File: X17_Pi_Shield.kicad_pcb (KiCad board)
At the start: 2 copper layers, 85 x 56 mm, 89 parts, among them J1 BM04B-GHS-TBT, J10 BM04B-GHS-TBT, J11 BM04B-GHS-TBT, J12 Conn_01x05_Pin, J13 Conn_01x03_Pin, J2 BM02B-GHS-TBT, J20 Conn_01x02_Pin, J22 430450212, J23 430450612, J24 430450212, J3 BM02B-GHS-TBT, J4 BM02B-GHS-TBT, J5 BM02B-GHS-TBT, J6 Conn_01x03_Pin, J7 BM04B-GHS-TBT, J8 UJC-HP-L-G-5-MSMT-TR, J9 Conn_01x03_Pin, U1 4754, U10 4754, U2 TPS2117DRLR, U3 INA260AIPW, U4 AZ1117IH-3.3TRG1, U5 MAX485, U6 MMBT3906LT3G, U7 ISOW1432BDFMR, U8 RASPBERRY_PI_4B_4GB

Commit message: Bruh
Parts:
- moved U3 0.52 mm to (175.2, 104.3)
- moved 3.3V 0.22 mm to (159.4, 94.9)
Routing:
- net GND: track 53.5 -> 120.5 mm, vias 0 -> 24
- net +3V3: track 205.7 -> 236.6 mm
- net /Pi + IMU/SCL: track 203.3 -> 210.2 mm
- net /UART/A: track 26.4 -> 32.9 mm
- net /Pi + IMU/SDA: track 186.4 -> 191.5 mm
- net +5V: track 159.4 -> 163.0 mm
- net /Pi + IMU/BKP_EN: track 78.2 -> 81.2 mm
- net Net-(U2-PR1): track 2.03 -> 4.75 mm
- net /Power/5V_TOTAL: track 44.9 -> 46.8 mm, vias 4 -> 6
- net Net-(D7-A): track 0.00 -> 1.94 mm
- net /Power/5V_BACKPLANE: track 47.2 -> 48.2 mm
- net /Power/Vs: track 22.6 -> 21.8 mm
- net /Pi + IMU/CE0: track 39.3 -> 40.1 mm
- net Net-(JP1-B): track 16.0 -> 15.3 mm
- net (no net): track 0.00 -> 0.62 mm

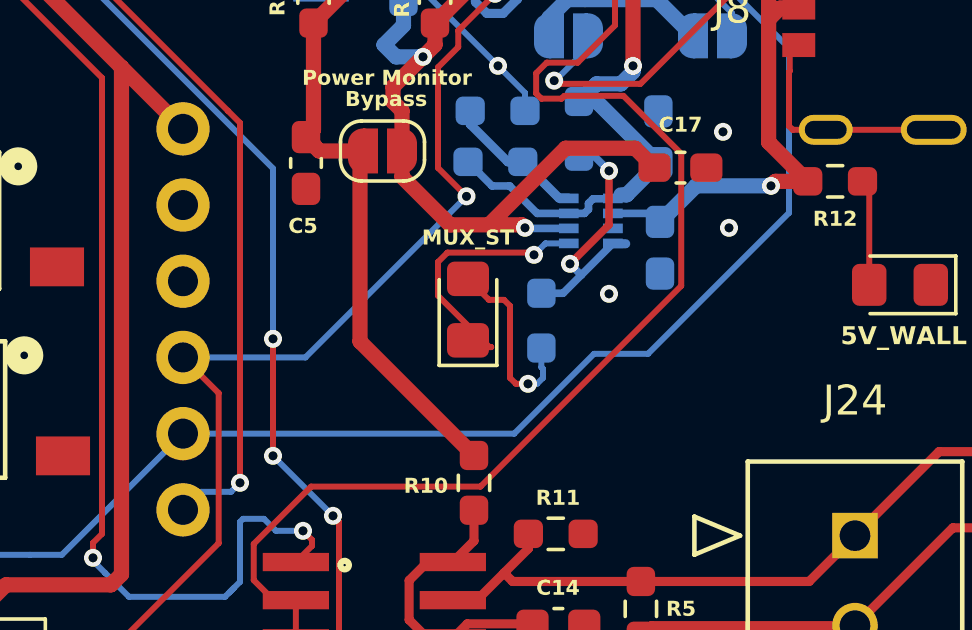
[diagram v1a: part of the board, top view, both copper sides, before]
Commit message: Unconnected Fix
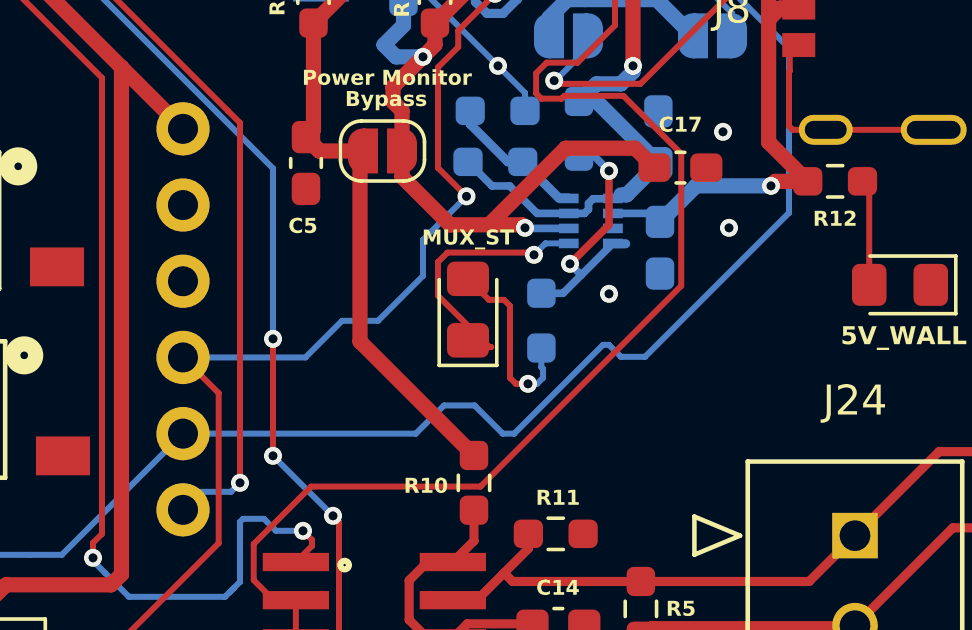
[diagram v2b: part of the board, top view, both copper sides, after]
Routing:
- net /Pi + IMU/SDA: track 191.5 -> 192.6 mm
- net /Pi + IMU/SCL: track 210.2 -> 210.9 mm
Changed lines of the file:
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@@
 	)
 	(segment
+		(start 175.1 119.7)
+		(end 175.3 119.7)
+		(width 0.2)
+		(layer "B.Cu")
+		(net 21)
+	)
+	(segment
 		(start 140.71 85.04)
 		(end 137.55 88.2)
@@
 	)
 	(segment
+		(start 181.3 109.805)
+		(end 178.07 106.575)
+		(width 0.2)
+		(layer "B.Cu")
+		(net 21)
+	)
+	(segment
+		(start 161.1 122.66)
+		(end 168.86 122.66)
+		(width 0.2)
+		(layer "B.Cu")
+		(net 21)
+	)
+	(segment
 		(start 110.3 112.5)
 		(end 111.4 111.4)
@@
 	)
 	(segment
-		(start 174.8 120)
-		(end 176.6 120)
+		(start 176.5 120.1)
+		(end 181.3 115.3)
+		(width 0.2)
+		(layer "B.Cu")
+		(net 21)
+	)
+	(segment
+		(start 168.86 122.66)
+		(end 169.8 121.72)
 		(width 0.2)
 		(layer "B.Cu")
@@
 	)
 	(segment
+		(start 171.76 122.66)
+		(end 172.14 122.66)
+		(width 0.2)
+		(layer "B.Cu")
+		(net 21)
+	)
+	(segment
 		(start 123.9 127.1)
 		(end 119 127.1)
@@
 	)
 	(segment
-		(start 129.4 88.2)
-		(end 127.6 90)
-		(width 0.254)
+		(start 169.8 121.72)
+		(end 170.82 121.72)
+		(width 0.2)
 		(layer "B.Cu")
 		(net 21)
 	)
 	(segment
-		(start 115.45 126.05)
-		(end 115.4 126)
+		(start 181.3 115.3)
+		(end 181.3 109.805)
 		(width 0.2)
 		(layer "B.Cu")
@@
 	)
 	(segment
-		(start 181.3 115.3)
-		(end 181.3 109.805)
-		(width 0.2)
+		(start 129.4 88.2)
+		(end 127.6 90)
+		(width 0.254)
 		(layer "B.Cu")
 		(net 21)
 	)
 	(segment
-		(start 161.1 122.66)
-		(end 172.14 122.66)
+		(start 115.45 126.05)
+		(end 115.4 126)
 		(width 0.2)
 		(layer "B.Cu")
@@
 	)
 	(segment
-		(start 115.5 111.6)
-		(end 115.6 111.6)
+		(start 175.3 119.7)
+		(end 175.7 120.1)
 		(width 0.2)
 		(layer "B.Cu")
@@
 	)
 	(segment
-		(start 136.04 119.26)
-		(end 137.5 119.26)
+		(start 172.14 122.66)
+		(end 175.1 119.7)
 		(width 0.2)
 		(layer "B.Cu")
@@
 	)
 	(segment
-		(start 117.1 127.7)
-		(end 115.45 126.05)
+		(start 115.5 111.6)
+		(end 115.6 111.6)
 		(width 0.2)
 		(layer "B.Cu")
@@
 	)
 	(segment
-		(start 181.3 109.805)
-		(end 178.07 106.575)
+		(start 175.7 120.1)
+		(end 176.5 120.1)
 		(width 0.2)
 		(layer "B.Cu")
@@
 	)
 	(segment
-		(start 117.9 127.1)
-		(end 117.3 127.7)
+		(start 136.04 119.26)
+		(end 137.5 119.26)
 		(width 0.2)
 		(layer "B.Cu")
@@
 	)
 	(segment
-		(start 172.14 122.66)
-		(end 174.8 120)
+		(start 170.82 121.72)
+		(end 171.76 122.66)
 		(width 0.2)
 		(layer "B.Cu")
@@
 	)
 	(segment
-		(start 176.6 120)
-		(end 181.3 115.3)
+		(start 117.1 127.7)
+		(end 115.45 126.05)
+		(width 0.2)
+		(layer "B.Cu")
+		(net 21)
+	)
+	(segment
+		(start 117.9 127.1)
+		(end 117.3 127.7)
 		(width 0.2)
 		(layer "B.Cu")
@@
 	)
 	(segment
+		(start 167.6 118.9)
+		(end 169.1 117.4)
+		(width 0.2)
+		(layer "B.Cu")
+		(net 22)
+	)
+	(segment
 		(start 130.9228 83.9772)
 		(end 134.6772 83.9772)
@@
 	)
 	(segment
+		(start 169.1 117.4)
+		(end 169.1 116.2)
+		(width 0.2)
+		(layer "B.Cu")
+		(net 22)
+	)
+	(segment
 		(start 142.2126 84.0026)
 		(end 143.25 85.04)
@@
 	)
 	(segment
-		(start 170.55 114.75)
-		(end 165.18 120.12)
+		(start 165.18 120.12)
+		(end 166.4 118.9)
 		(width 0.2)
 		(layer "B.Cu")
@@
 	)
 	(segment
-		(start 165.18 120.12)
-		(end 161.1 120.12)
+		(start 117.5 104.6)
+		(end 117.5 104.3)
+		(width 0.254)
+		(layer "B.Cu")
+		(net 22)
+	)
+	(segment
+		(start 161.1 120.12)
+		(end 165.18 120.12)
 		(width 0.2)
 		(layer "B.Cu")
@@
 	)
 	(segment
-		(start 117.5 104.6)
-		(end 117.5 104.3)
-		(width 0.254)
+		(start 166.4 118.9)
+		(end 167.6 118.9)
+		(width 0.2)
 		(layer "B.Cu")
 		(net 22)
@@
 	)
 	(segment
+		(start 169.1 116.2)
+		(end 170.55 114.75)
+		(width 0.2)
+		(layer "B.Cu")
+		(net 22)
+	)
+	(segment
 		(start 117.2 104)
 		(end 116.9 104)
@@
 	)
 	(segment
-		(start 153.41 97.39)
-		(end 153.3 97.5)
+		(start 145.7 110.9)
+		(end 145.7 119)
 		(width 0.2)
 		(layer "B.Cu")
@@
 	)
 	(segment
-		(start 151.3 105.3)
-		(end 145.7 110.9)
+		(start 153.41 97.39)
+		(end 153.3 97.5)
 		(width 0.2)
 		(layer "B.Cu")
@@
 	)
 	(segment
-		(start 145.7 110.9)
-		(end 145.7 119)
+		(start 151.3 105.3)
+		(end 145.7 110.9)
 		(width 0.2)
 		(layer "B.Cu")
@@
 	)
 	(segment
-		(start 143.94 119.5)
-		(end 143.32 120.12)
+		(start 145.2 119.5)
+		(end 143.94 119.5)
 		(width 0.2)
 		(layer "B.Cu")
@@
 	)
 	(segment
-		(start 153.41 85.04)
-		(end 153.41 97.39)
+		(start 151.3 104)
+		(end 151.3 105.3)
 		(width 0.2)
 		(layer "B.Cu")
@@
 	)
 	(segment
-		(start 145.7 119)
-		(end 145.2 119.5)
+		(start 143.94 119.5)
+		(end 143.32 120.12)
 		(width 0.2)
 		(layer "B.Cu")
@@
 	)
 	(segment
-		(start 145.2 119.5)
-		(end 143.94 119.5)
+		(start 153.41 85.04)
+		(end 153.41 97.39)
 		(width 0.2)
 		(layer "B.Cu")
@@
 	)
 	(segment
-		(start 151.3 104)
-		(end 151.3 105.3)
+		(start 145.7 119)
+		(end 145.2 119.5)
 		(width 0.2)
 		(layer "B.Cu")

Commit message: Pre Design Review - Reviewed DRC Errors
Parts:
- removed C21: 22uF, Capacitor_SMD:C_0603_1608Metric_Pad1.08x0.95mm_HandSolder
- removed U4: AZ1117IH-3.3TRG1, AZ1117IH_3_3TRG1:SOT223_AZ1117I_6P5X3P5_DIO-M
- added C11: 10uF, Capacitor_SMD:C_0603_1608Metric_Pad1.08x0.95mm_HandSolder, B.Cu at (166.7, 107.1)
- added U9: AZ1117IH-3.3TRG1, AZ1117IH_3_3TRG1 (3):SOT230P700X185-4N, B.Cu at (161.3, 105.4)
- C18: value 10uF -> 22uF
- JP3: renamed from Power Monitor
- moved C18 4.16 mm to (166.7, 103.6)
- renumbered 3.3V to +3V3, 5V to +5V, LEAK to D1, MUX_ST to D2, 5V_WALL to D4, 5V_TOTAL to D5, 5V_BKP to D6, 5V to D7, 3.3V to D8, A1 to JP1, A0 to JP2, MUX to JP4
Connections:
- C18 pad 1: /Power/5V_TOTAL -> /Power/Vs
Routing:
- net /Power/Vs: track 21.8 -> 33.2 mm
- net GND: track 120.5 -> 126.0 mm, vias 24 -> 25
- net /Power/5V_TOTAL: track 46.8 -> 48.2 mm
- net (no net): track 0.62 -> 0.00 mm

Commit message: Pre 4 Layer Routing
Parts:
- moved J2 2.85 mm to (128.9, 113.3)
- moved J3 2.35 mm to (152.0, 113.2)
- moved D2 0.30 mm to (170.6, 118.8), turned to -90 degrees
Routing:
- net /Sensors/PROBE: track 41.6 -> 46.5 mm
- net GND: track 126.0 -> 121.5 mm
- net Net-(D2-A): track 6.46 -> 4.41 mm
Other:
- copper layers 2 -> 4
